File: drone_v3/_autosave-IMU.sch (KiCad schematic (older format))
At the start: 19 parts, among them J2 Conn_01x10_Female, U3 MPU-9250, U4 MCP1700-3302E_SOT23, U7 MS5611-01BA, U8 ICM-20602

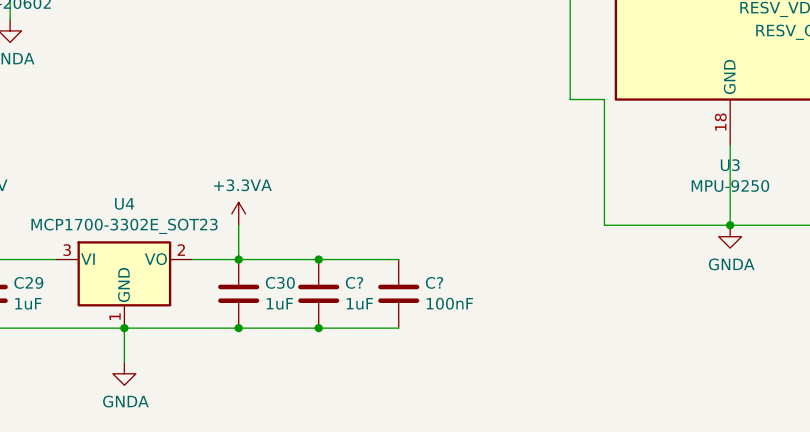
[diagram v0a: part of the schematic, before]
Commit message: test analog split
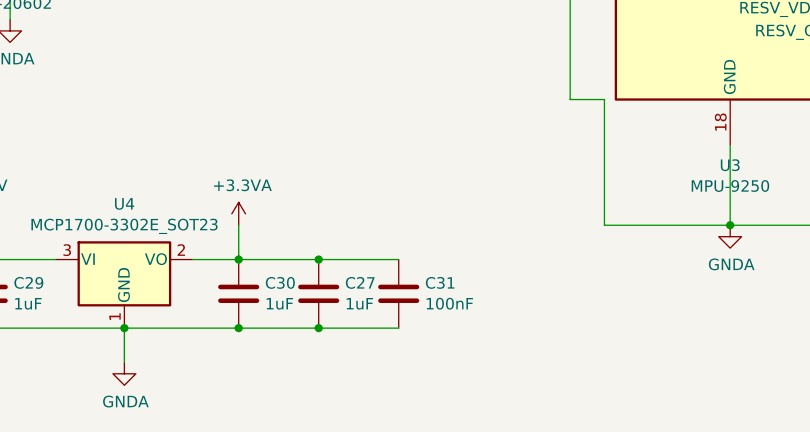
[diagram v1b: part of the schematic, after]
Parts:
- gave numbers to parts that had none: 2
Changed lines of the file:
@@
 AR Path="/5F3C8D97" Ref="C?"  Part="1"
 AR Path="/5F569749/5F3C8D97" Ref="C?"  Part="1"
-AR Path="/5F3218EE/5F3C8D97" Ref="C?"  Part="1"
-F 0 "C?" H 4215 5896 50  0000 L CNN
+AR Path="/5F3218EE/5F3C8D97" Ref="C27"  Part="1"
+F 0 "C27" H 4215 5896 50  0000 L CNN
 F 1 "1uF" H 4215 5805 50  0000 L CNN
 F 2 "Capacitor_SMD:C_0603_1608Metric_Pad1.05x0.95mm_HandSolder" H 4138 5700 50  0001 C CNN
@@
 AR Path="/5F3CBB6C" Ref="C?"  Part="1"
 AR Path="/5F569749/5F3CBB6C" Ref="C?"  Part="1"
-AR Path="/5F3218EE/5F3CBB6C" Ref="C?"  Part="1"
-F 0 "C?" H 4565 5896 50  0000 L CNN
+AR Path="/5F3218EE/5F3CBB6C" Ref="C31"  Part="1"
+F 0 "C31" H 4565 5896 50  0000 L CNN
 F 1 "100nF" H 4565 5805 50  0000 L CNN
 F 2 "Capacitor_SMD:C_0603_1608Metric_Pad1.05x0.95mm_HandSolder" H 4488 5700 50  0001 C CNN
